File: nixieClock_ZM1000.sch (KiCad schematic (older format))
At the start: 4 parts

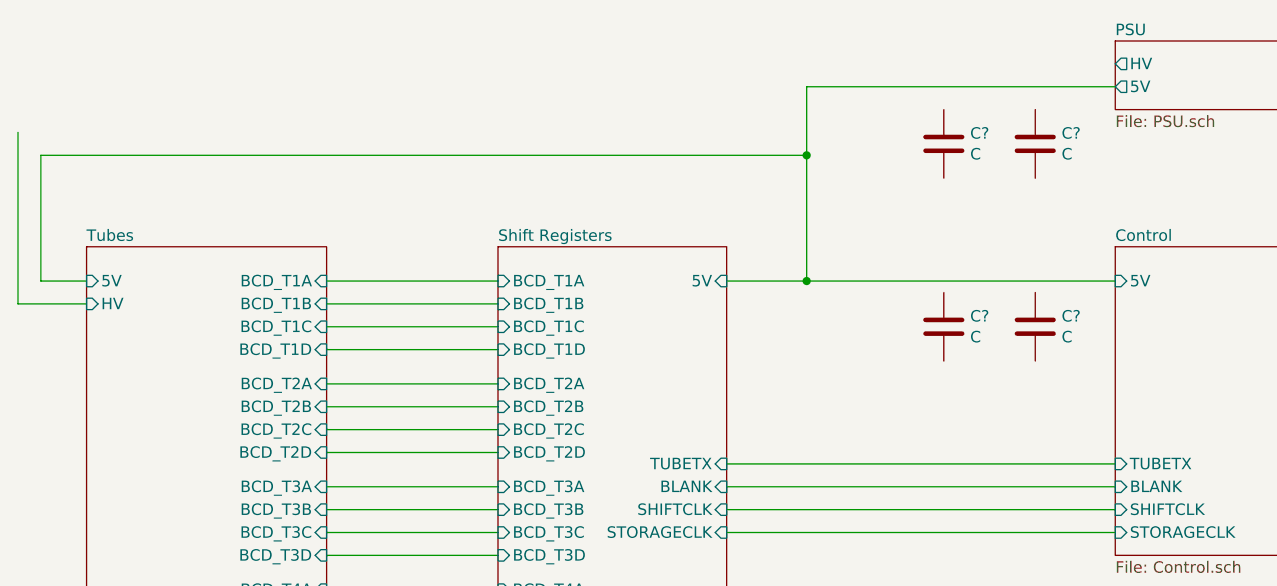
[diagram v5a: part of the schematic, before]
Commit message: Added more decoupling
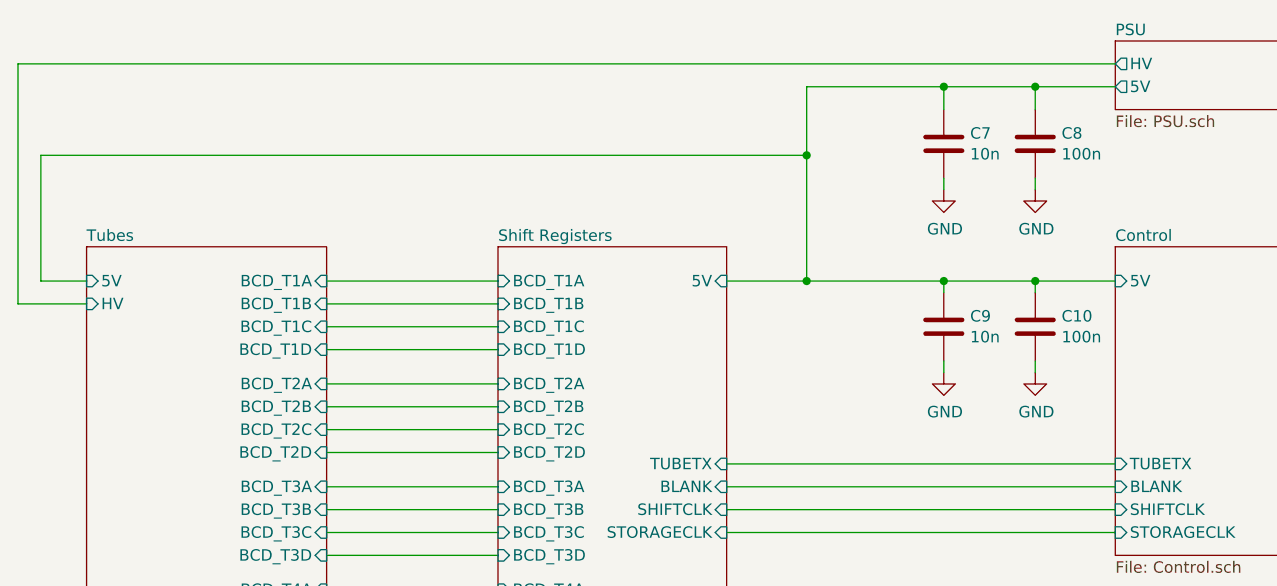
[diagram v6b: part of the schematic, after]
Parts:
- C10, C8: renamed from C?; value C -> 100n; footprint (none) -> Capacitor_THT:C_Disc_D5.0mm_W2.5mm_P2.50mm
- C7, C9: renamed from C?; value C -> 10n; footprint (none) -> Capacitor_THT:C_Disc_D3.8mm_W2.6mm_P2.50mm
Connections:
- net Control/5V: now also C10.1, C7.1, C8.1, C9.1
- net GND: now reaches C10.2
- net GND: now also C7.2, C8.2, C9.2
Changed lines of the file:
@@
 	3400 2150 3400 2700
-Wire Wire Line
-	3300 2050 3300 2800
 Wire Wire Line
 	4650 5500 5400 5500
@@
 	8100 3500 6400 3500
 Wire Wire Line
-	6750 2700 8100 2700
+	6750 2700 7350 2700
 Wire Wire Line
 	3400 2150 6750 2150
@@
 	6750 2150 6750 1850
 Wire Wire Line
-	6750 1850 8100 1850
+	6750 1850 7350 1850
 Connection ~ 6750 2150
 $Comp
-L Device:C C?
+L Device:C C10
 U 1 1 5DA9F019
 P 7750 2900
-F 0 "C?" H 7865 2946 50  0000 L CNN
-F 1 "C" H 7865 2855 50  0000 L CNN
-F 2 "" H 7788 2750 50  0001 C CNN
+F 0 "C10" H 7865 2946 50  0000 L CNN
+F 1 "100n" H 7865 2855 50  0000 L CNN
+F 2 "Capacitor_THT:C_Disc_D5.0mm_W2.5mm_P2.50mm" H 7788 2750 50  0001 C CNN
 F 3 "~" H 7750 2900 50  0001 C CNN
 	1    7750 2900
@@
 $EndComp
 $Comp
-L Device:C C?
+L Device:C C9
 U 1 1 5DA9F705
 P 7350 2900
-F 0 "C?" H 7465 2946 50  0000 L CNN
-F 1 "C" H 7465 2855 50  0000 L CNN
-F 2 "" H 7388 2750 50  0001 C CNN
+F 0 "C9" H 7465 2946 50  0000 L CNN
+F 1 "10n" H 7465 2855 50  0000 L CNN
+F 2 "Capacitor_THT:C_Disc_D3.8mm_W2.6mm_P2.50mm" H 7388 2750 50  0001 C CNN
 F 3 "~" H 7350 2900 50  0001 C CNN
 	1    7350 2900
@@
 $EndComp
 $Comp
-L Device:C C?
+L Device:C C8
 U 1 1 5DAA0435
 P 7750 2100
-F 0 "C?" H 7865 2146 50  0000 L CNN
-F 1 "C" H 7865 2055 50  0000 L CNN
-F 2 "" H 7788 1950 50  0001 C CNN
+F 0 "C8" H 7865 2146 50  0000 L CNN
+F 1 "100n" H 7865 2055 50  0000 L CNN
+F 2 "Capacitor_THT:C_Disc_D5.0mm_W2.5mm_P2.50mm" H 7788 1950 50  0001 C CNN
 F 3 "~" H 7750 2100 50  0001 C CNN
 	1    7750 2100
@@
 $EndComp
 $Comp
-L Device:C C?
+L Device:C C7
 U 1 1 5DAA043B
 P 7350 2100
-F 0 "C?" H 7465 2146 50  0000 L CNN
-F 1 "C" H 7465 2055 50  0000 L CNN
-F 2 "" H 7388 1950 50  0001 C CNN
+F 0 "C7" H 7465 2146 50  0000 L CNN
+F 1 "10n" H 7465 2055 50  0000 L CNN
+F 2 "Capacitor_THT:C_Disc_D3.8mm_W2.6mm_P2.50mm" H 7388 1950 50  0001 C CNN
 F 3 "~" H 7350 2100 50  0001 C CNN
 	1    7350 2100
 	1    0    0    -1
 $EndComp
+$Comp
+L power:GND #PWR0101
+U 1 1 5D98D268
+P 7750 2300
+F 0 "#PWR0101" H 7750 2050 50  0001 C CNN
+F 1 "GND" H 7755 2127 50  0000 C CNN
+F 2 "" H 7750 2300 50  0001 C CNN
+F 3 "" H 7750 2300 50  0001 C CNN
+	1    7750 2300
+	1    0    0    -1
+$EndComp
+$Comp
+L power:GND #PWR0102
+U 1 1 5D98D5C7
+P 7350 2300
+F 0 "#PWR0102" H 7350 2050 50  0001 C CNN
+F 1 "GND" H 7355 2127 50  0000 C CNN
+F 2 "" H 7350 2300 50  0001 C CNN
+F 3 "" H 7350 2300 50  0001 C CNN
+	1    7350 2300
+	1    0    0    -1
+$EndComp
+$Comp
+L power:GND #PWR0103
+U 1 1 5D98E1B2
+P 7750 3100
+F 0 "#PWR0103" H 7750 2850 50  0001 C CNN
+F 1 "GND" H 7755 2927 50  0000 C CNN
+F 2 "" H 7750 3100 50  0001 C CNN
+F 3 "" H 7750 3100 50  0001 C CNN
+	1    7750 3100
+	1    0    0    -1
+$EndComp
+$Comp
+L power:GND #PWR0104
+U 1 1 5D98E1B8
+P 7350 3100
+F 0 "#PWR0104" H 7350 2850 50  0001 C CNN
+F 1 "GND" H 7355 2927 50  0000 C CNN
+F 2 "" H 7350 3100 50  0001 C CNN
+F 3 "" H 7350 3100 50  0001 C CNN
+	1    7350 3100
+	1    0    0    -1
+$EndComp
+Wire Wire Line
+	7350 3100 7350 3050
+Wire Wire Line
+	7750 3100 7750 3050
+Wire Wire Line
+	7750 2750 7750 2700
+Connection ~ 7750 2700
+Wire Wire Line
+	7750 2700 8100 2700
+Wire Wire Line
+	7350 2750 7350 2700
+Connection ~ 7350 2700
+Wire Wire Line
+	7350 2700 7750 2700
+Wire Wire Line
+	7350 2250 7350 2300
+Wire Wire Line
+	7350 1950 7350 1850
+Connection ~ 7350 1850
+Wire Wire Line
+	7350 1850 7750 1850
+Wire Wire Line
+	7750 1950 7750 1850
+Connection ~ 7750 1850
+Wire Wire Line
+	7750 1850 8100 1850
+Wire Wire Line
+	7750 2250 7750 2300
+Wire Wire Line
+	8100 1750 3300 1750
+Wire Wire Line
+	3300 1750 3300 2800
 $EndSCHEMATC

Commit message: Fixed tube footprints and rerouted
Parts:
- renumbered C7 to C1, C9 to C2, C8 to C3, C10 to C4
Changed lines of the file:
@@
 EESchema Schematic File Version 4
-LIBS:nixieClock_ZM1000-cache
 EELAYER 30 0
 EELAYER END
@@
 Connection ~ 6750 2150
 $Comp
-L Device:C C10
+L Device:C C4
 U 1 1 5DA9F019
 P 7750 2900
-F 0 "C10" H 7865 2946 50  0000 L CNN
+F 0 "C4" H 7865 2946 50  0000 L CNN
 F 1 "100n" H 7865 2855 50  0000 L CNN
 F 2 "Capacitor_THT:C_Disc_D5.0mm_W2.5mm_P2.50mm" H 7788 2750 50  0001 C CNN
@@
 $EndComp
 $Comp
-L Device:C C9
+L Device:C C2
 U 1 1 5DA9F705
 P 7350 2900
-F 0 "C9" H 7465 2946 50  0000 L CNN
+F 0 "C2" H 7465 2946 50  0000 L CNN
 F 1 "10n" H 7465 2855 50  0000 L CNN
 F 2 "Capacitor_THT:C_Disc_D3.8mm_W2.6mm_P2.50mm" H 7388 2750 50  0001 C CNN
@@
 $EndComp
 $Comp
-L Device:C C8
+L Device:C C3
 U 1 1 5DAA0435
 P 7750 2100
-F 0 "C8" H 7865 2146 50  0000 L CNN
+F 0 "C3" H 7865 2146 50  0000 L CNN
 F 1 "100n" H 7865 2055 50  0000 L CNN
 F 2 "Capacitor_THT:C_Disc_D5.0mm_W2.5mm_P2.50mm" H 7788 1950 50  0001 C CNN
@@
 $EndComp
 $Comp
-L Device:C C7
+L Device:C C1
 U 1 1 5DAA043B
 P 7350 2100
-F 0 "C7" H 7465 2146 50  0000 L CNN
+F 0 "C1" H 7465 2146 50  0000 L CNN
 F 1 "10n" H 7465 2055 50  0000 L CNN
 F 2 "Capacitor_THT:C_Disc_D3.8mm_W2.6mm_P2.50mm" H 7388 1950 50  0001 C CNN
@@
 $EndComp
 $Comp
-L power:GND #PWR0101
+L power:GND #PWR03
 U 1 1 5D98D268
 P 7750 2300
-F 0 "#PWR0101" H 7750 2050 50  0001 C CNN
+F 0 "#PWR03" H 7750 2050 50  0001 C CNN
 F 1 "GND" H 7755 2127 50  0000 C CNN
 F 2 "" H 7750 2300 50  0001 C CNN
@@
 $EndComp
 $Comp
-L power:GND #PWR0102
+L power:GND #PWR01
 U 1 1 5D98D5C7
 P 7350 2300
-F 0 "#PWR0102" H 7350 2050 50  0001 C CNN
+F 0 "#PWR01" H 7350 2050 50  0001 C CNN
 F 1 "GND" H 7355 2127 50  0000 C CNN
 F 2 "" H 7350 2300 50  0001 C CNN
@@
 $EndComp
 $Comp
-L power:GND #PWR0103
+L power:GND #PWR04
 U 1 1 5D98E1B2
 P 7750 3100
-F 0 "#PWR0103" H 7750 2850 50  0001 C CNN
+F 0 "#PWR04" H 7750 2850 50  0001 C CNN
 F 1 "GND" H 7755 2927 50  0000 C CNN
 F 2 "" H 7750 3100 50  0001 C CNN
@@
 $EndComp
 $Comp
-L power:GND #PWR0104
+L power:GND #PWR02
 U 1 1 5D98E1B8
 P 7350 3100
-F 0 "#PWR0104" H 7350 2850 50  0001 C CNN
+F 0 "#PWR02" H 7350 2850 50  0001 C CNN
 F 1 "GND" H 7355 2927 50  0000 C CNN
 F 2 "" H 7350 3100 50  0001 C CNN
